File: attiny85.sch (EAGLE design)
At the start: 8 parts, among them U1 TINY85-20-DIP

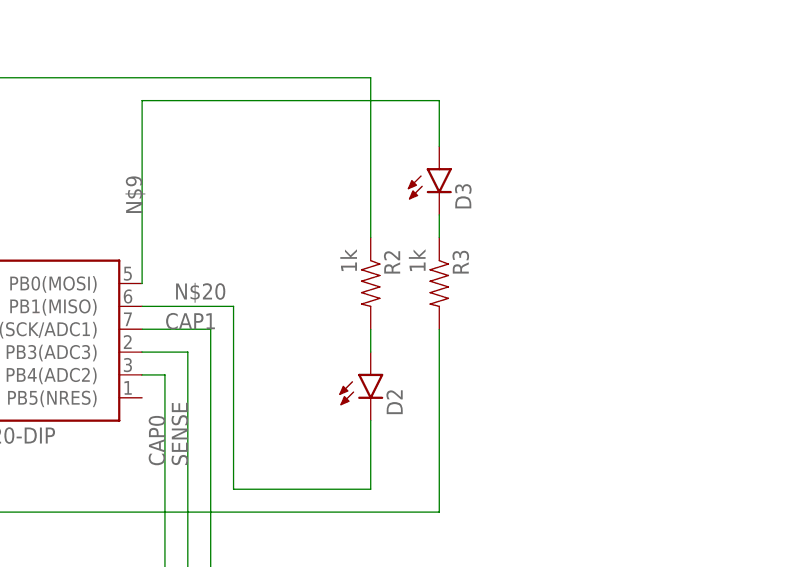
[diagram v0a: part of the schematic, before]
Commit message: Minor Cleanups - Silkscreen & Battery Holder
Battery Holder: Updated so that the rest of the plane isn't also
		exposed on the board

Silkscreen: mostly minor adjustments, and exposing the right led
		resistor
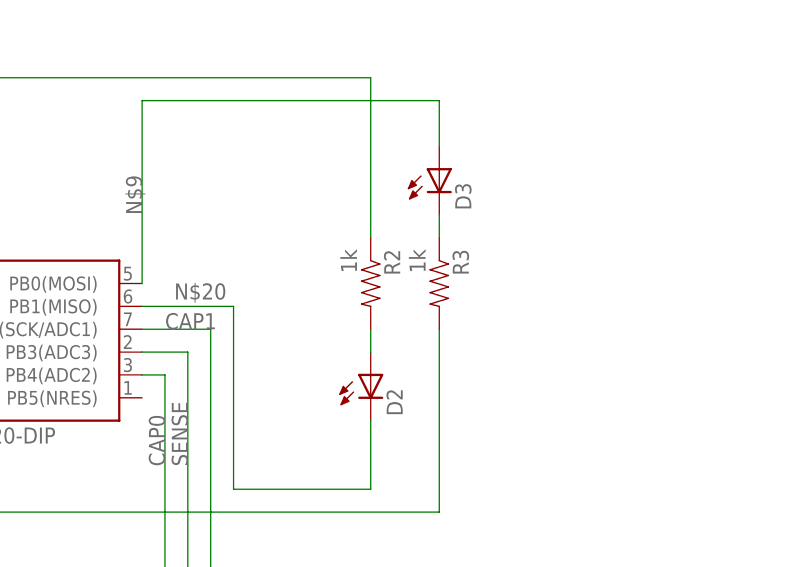
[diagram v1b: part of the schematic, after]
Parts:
- BAT1: device adafruit:CR2032THM -> adafruit-john modded:CR2032THM
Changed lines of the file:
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@@
 <?xml version="1.0" encoding="utf-8"?>
 <!DOCTYPE eagle SYSTEM "eagle.dtd">
-<eagle version="7.6.0">
+<eagle version="7.7.0">
 <drawing>
 <settings>
@@
 <part name="R17" library="SparkFun-Resistors" deviceset="1KOHM-1/4W-5%(PTH)" device="" value="1M"/>
 <part name="R18" library="SparkFun-Resistors" deviceset="1KOHM-1/4W-5%(PTH)" device="" value="1M"/>
-<part name="BAT1" library="adafruit" deviceset="CR2032" device="THM"/>
+<part name="BAT1" library="adafruit-john modded" deviceset="CR2032" device="THM"/>
 </parts>
 <sheets>
